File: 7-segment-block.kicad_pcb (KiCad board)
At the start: 2 copper layers, 90 x 47.8 mm, 27 parts, among them J1 DATA_OUT, J2 DATA_IN, U1 TPIC6C596PWR, U2 74LS243

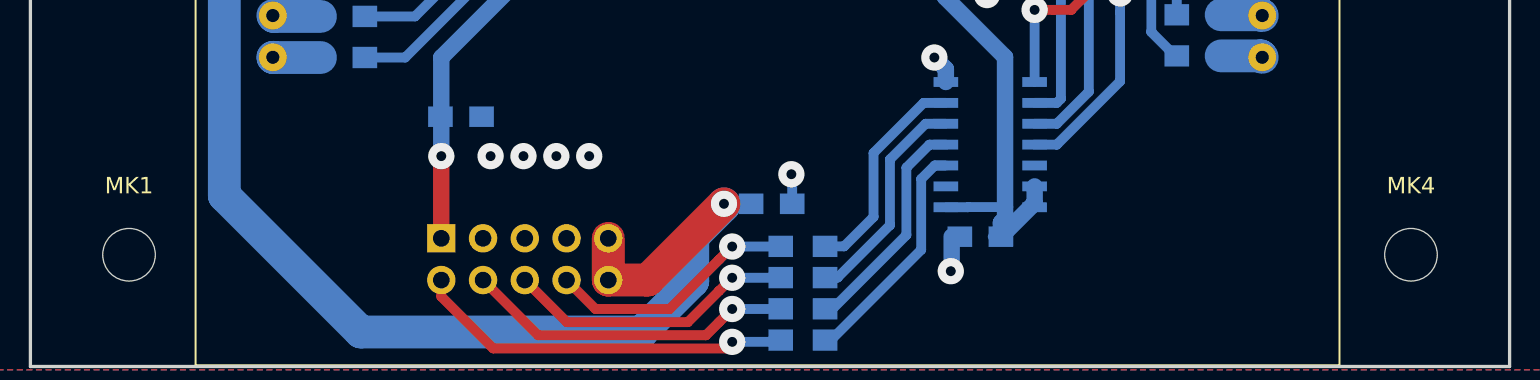
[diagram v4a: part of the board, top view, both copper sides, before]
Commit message: Change orientation of cap to mitigate bendring problems. Add dimensions and hole markers
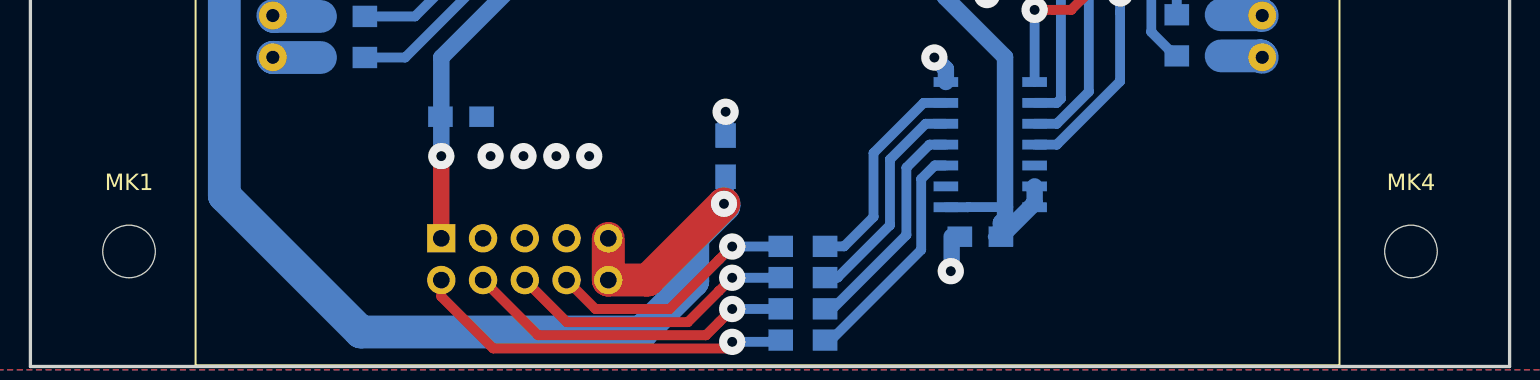
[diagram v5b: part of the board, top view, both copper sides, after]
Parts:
- moved C6 4.03 mm to (158.3, 79.0), turned to 90 degrees
- moved MK1 0.20 mm to (122.0, 84.8)
- moved MK4 0.20 mm to (200.0, 84.8)

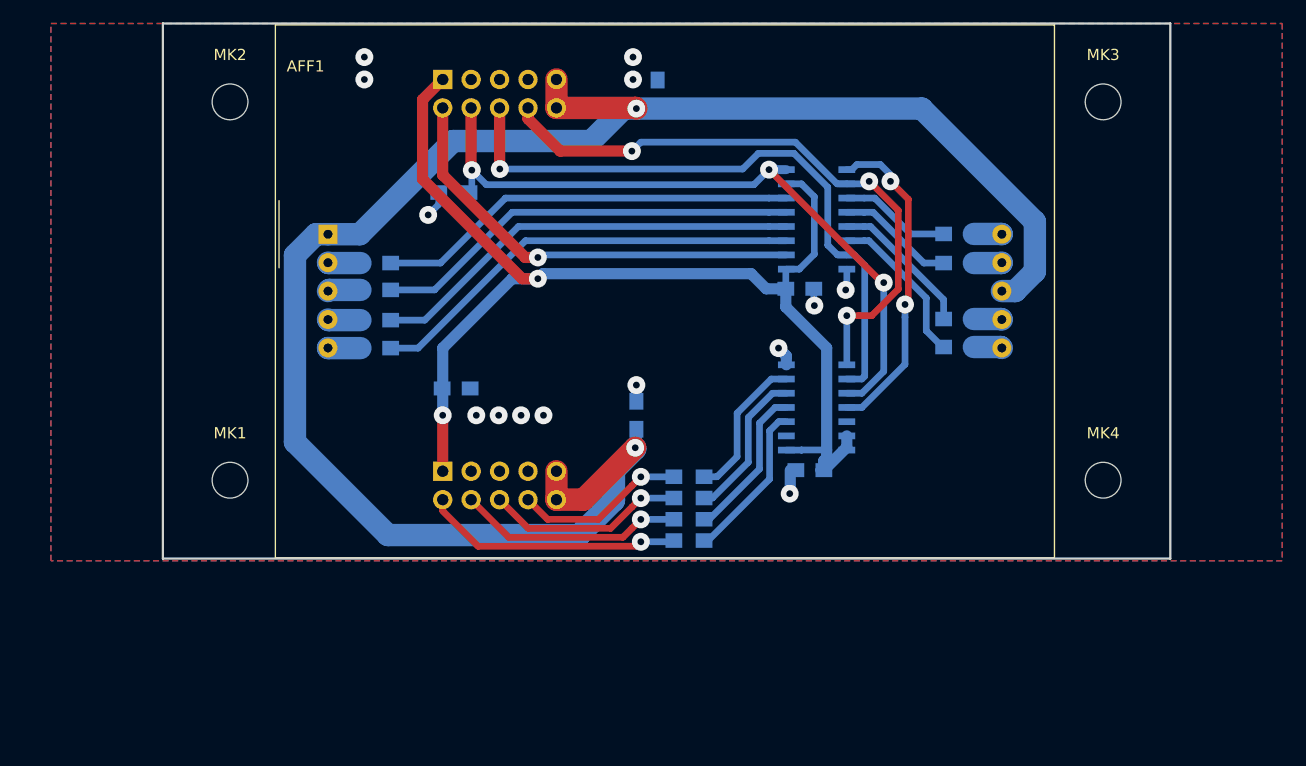
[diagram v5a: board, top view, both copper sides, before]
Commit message: Add pullup on ~G, send for manufacturing
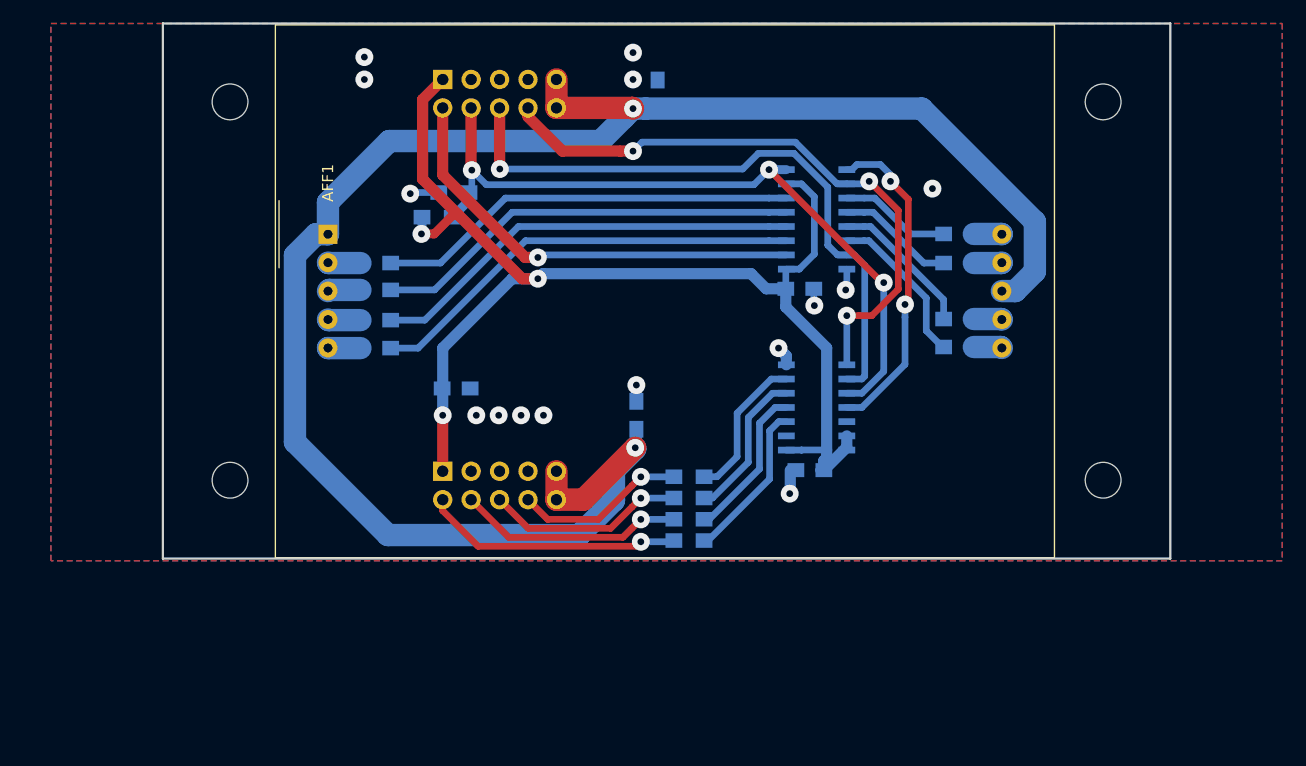
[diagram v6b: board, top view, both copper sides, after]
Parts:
- added R14: 10k, Resistors_SMD:R_0805_HandSoldering, B.Cu at (140.5, 61.3)
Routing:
- net +5V: track 113.8 -> 119.4 mm, vias 2 -> 3
- net /~G: track 63.4 -> 66.2 mm
- net VCC: track 164.1 -> 165.7 mm
- net GND: track 11.2 -> 11.4 mm, vias 14 -> 15
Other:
- board text added: "+5V GND GND GND +12V"
- board text added: "7-segment block v1.1 2017 Albertas Mickenas mic@wemakethings.net"
- board text added: "DATA IN ~ENABLE CLOCK LATCH +12V"

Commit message: Add some lincence notices
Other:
- board text added: "Copyright 2017 Albertas Mickėnas Licensed under the Apache License, Version 2.0 (the "License"); you may not use this file except in compliance with the License. You may obtain a copy of the License at http://www.apache.org/licenses/LICENSE-2.0 Unless required by applicable law or agreed to in writing, software distributed under the License is distributed on an "AS IS" BASIS, WITHOUT WARRANTIES O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"
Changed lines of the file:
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@@
   (general
     (thickness 1.6)
-    (drawings 18)
+    (drawings 19)
     (tracks 276)
     (zones 0)
@@
     (46 B.CrtYd user)
     (47 F.CrtYd user)
-    (48 B.Fab user hide)
+    (48 B.Fab user)
     (49 F.Fab user)
   )
@@
       (drillshape 0)
       (scaleselection 1)
-      (outputdirectory ./gerbers))
+      (outputdirectory manufacturing/))
   )
   (net 0 "")
@@
     )
   )
+  (gr_text "Copyright 2017 Albertas Mickėnas\n\n   Licensed under the Apache License, Version 2.0 (the \"License\");\n   you may not use this file except in compliance with the License.\n   You may obtain a copy of the License at\n\n       http://www.apache.org/licenses/LICENSE-2.0\n\n   Unless required by applicable law or agreed to in writing, software\n   distributed under the License is distributed on an \"AS IS\" BASIS,\n   WITHOUT WARRANTIES OR CONDITIONS OF ANY KIND, either \n   express or implied.\n   See the License for the specific language governing permissions and \n   limitations under the License." (at 182.75 159) (layer Cmts.User)
+    (effects (font (size 1.5 1.5) (thickness 0.3)) (justify left))
+  )
   (gr_text "7-segment block v1.1\n2017 Albertas Mickenas\nmic@wemakethings.net" (at 199.5 68 90) (layer B.SilkS)
